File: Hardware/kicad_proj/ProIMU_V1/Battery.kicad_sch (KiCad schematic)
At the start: 19 parts, among them Q1 2SC4213

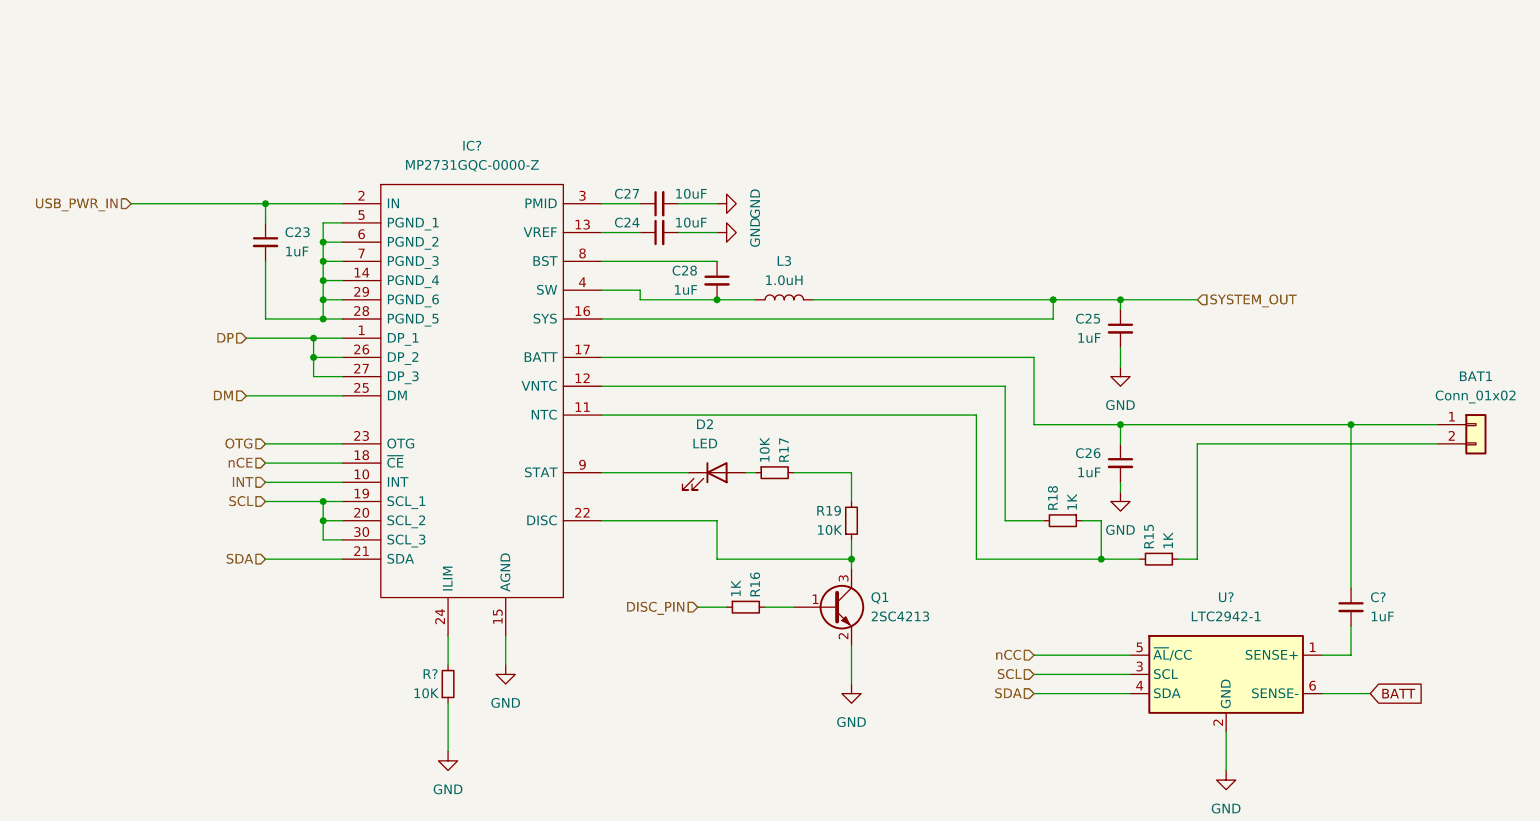
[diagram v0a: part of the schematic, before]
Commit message: Updated Schematic and Layout. RS232 and CAN connectors to be interchanged
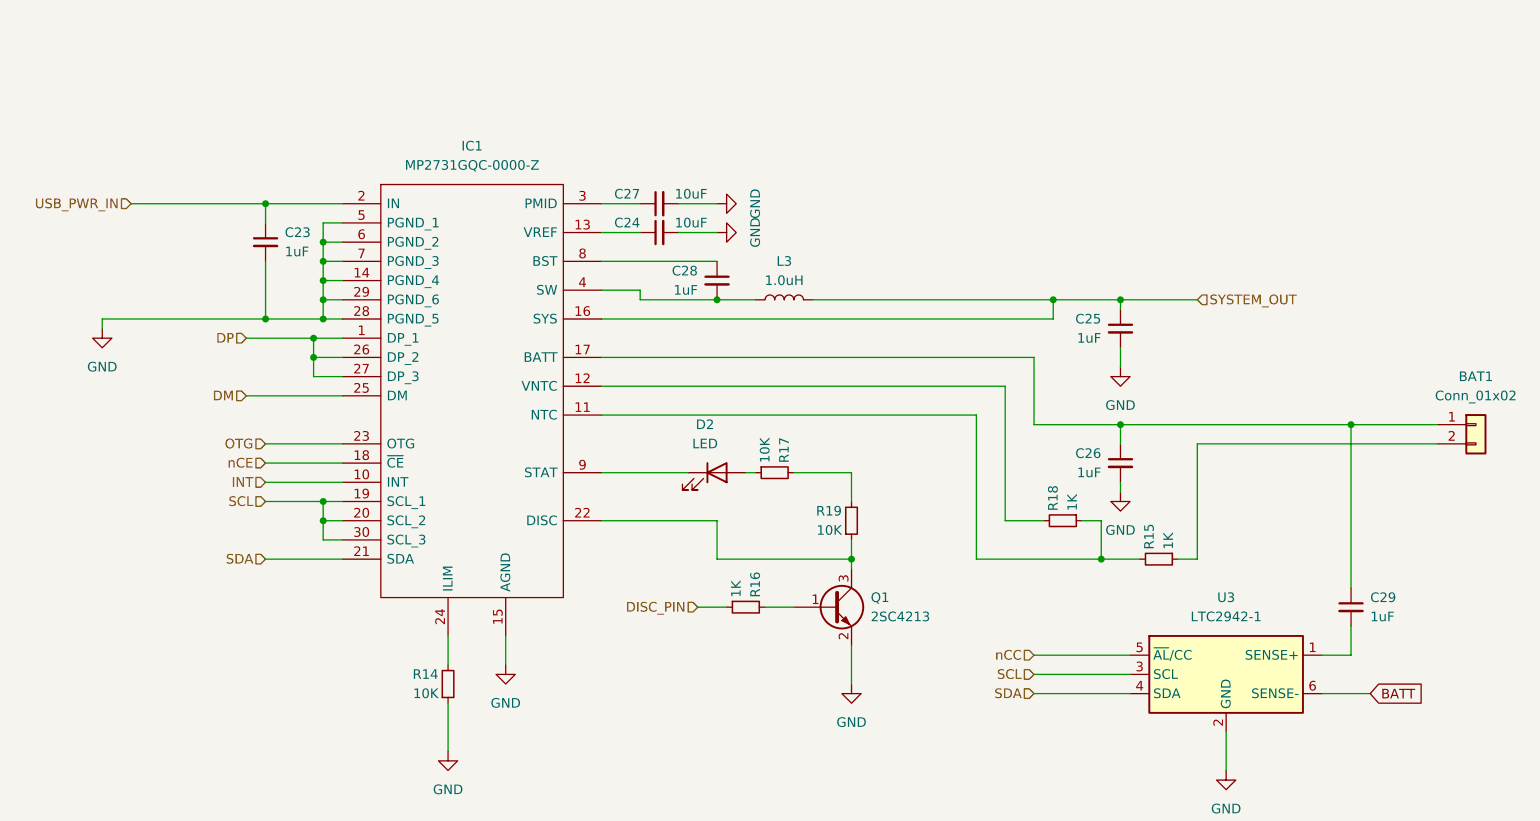
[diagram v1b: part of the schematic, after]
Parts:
- gave numbers to parts that had none: 4
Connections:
- net GND: now also C23.2, IC1.14 (PGND_4), IC1.28 (PGND_5), IC1.29 (PGND_6), IC1.5 (PGND_1), IC1.6 (PGND_2), IC1.7 (PGND_3)
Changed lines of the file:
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@@
   (junction (at 92.71 96.52) (diameter 0) (color 0 0 0 0)
   )
+  (junction (at 85.09 72.39) (diameter 0) (color 0 0 0 0)
+  )
   (junction (at 91.44 77.47) (diameter 0) (color 0 0 0 0)
   )
@@
     (stroke (width 0) (type default) (color 0 0 0 0))
   )
+  (wire (pts (xy 63.5 72.39) (xy 63.5 73.66))
+    (stroke (width 0) (type default) (color 0 0 0 0))
+  )
   (wire (pts (xy 142.24 110.49) (xy 146.05 110.49))
     (stroke (width 0) (type default) (color 0 0 0 0))
@@
   )
   (wire (pts (xy 92.71 64.77) (xy 92.71 67.31))
+    (stroke (width 0) (type default) (color 0 0 0 0))
+  )
+  (wire (pts (xy 85.09 72.39) (xy 63.5 72.39))
     (stroke (width 0) (type default) (color 0 0 0 0))
   )
@@
   (symbol (lib_id "power:GND") (at 212.09 132.08 0) (unit 1)
     (in_bom yes) (on_board yes) (fields_autoplaced)
-    (property "Reference" "#PWR?" (id 0) (at 212.09 138.43 0)
+    (property "Reference" "#PWR012" (id 0) (at 212.09 138.43 0)
       (effects (font (size 1.27 1.27)) hide)
     )
@@
     (pin "2")
   )
+  (symbol (lib_id "power:GND") (at 63.5 73.66 0) (unit 1)
+    (in_bom yes) (on_board yes) (fields_autoplaced)
+    (property "Reference" "#PWR08" (id 0) (at 63.5 80.01 0)
+      (effects (font (size 1.27 1.27)) hide)
+    )
+    (property "Value" "GND" (id 1) (at 63.5 78.74 0))
+    (property "Footprint" "" (id 2) (at 63.5 73.66 0)
+      (effects (font (size 1.27 1.27)) hide)
+    )
+    (property "Datasheet" "" (id 3) (at 63.5 73.66 0)
+      (effects (font (size 1.27 1.27)) hide)
+    )
+    (pin "1")
+  )
   (symbol (lib_id "Device:R_Small") (at 109.22 120.65 0) (mirror x) (unit 1)
     (in_bom yes) (on_board yes)
-    (property "Reference" "R?" (id 0) (at 107.95 119.38 0)
+    (property "Reference" "R14" (id 0) (at 107.95 119.38 0)
       (effects (font (size 1.27 1.27)) (justify right))
     )
@@
   (symbol (lib_id "power:GND") (at 116.84 118.11 0) (unit 1)
     (in_bom yes) (on_board yes) (fields_autoplaced)
-    (property "Reference" "#PWR?" (id 0) (at 116.84 124.46 0)
+    (property "Reference" "#PWR011" (id 0) (at 116.84 124.46 0)
       (effects (font (size 1.27 1.27)) hide)
     )
@@
   (symbol (lib_name "MP2731GQC-0000-Z_1") (lib_id "MP2731GQC-0000-Z:MP2731GQC-0000-Z") (at 96.52 57.15 0) (unit 1)
     (in_bom yes) (on_board yes) (fields_autoplaced)
-    (property "Reference" "IC?" (id 0) (at 112.395 49.53 0))
+    (property "Reference" "IC1" (id 0) (at 112.395 49.53 0))
     (property "Value" "MP2731GQC-0000-Z" (id 1) (at 112.395 52.07 0))
     (property "Footprint" "MP2731GQC0000Z" (id 2) (at 125.73 54.61 0)
@@
   (symbol (lib_id "Device:C_Small") (at 228.6 110.49 0) (unit 1)
     (in_bom yes) (on_board yes) (fields_autoplaced)
-    (property "Reference" "C?" (id 0) (at 231.14 109.2262 0)
+    (property "Reference" "C29" (id 0) (at 231.14 109.2262 0)
       (effects (font (size 1.27 1.27)) (justify left))
     )
@@
   (symbol (lib_id "Battery_Management:LTC2942-1") (at 212.09 119.38 0) (unit 1)
     (in_bom yes) (on_board yes) (fields_autoplaced)
-    (property "Reference" "U?" (id 0) (at 212.09 109.22 0))
+    (property "Reference" "U3" (id 0) (at 212.09 109.22 0))
     (property "Value" "LTC2942-1" (id 1) (at 212.09 111.76 0))
     (property "Footprint" "Package_DFN_QFN:DFN-6-1EP_3x2mm_P0.5mm_EP1.65x1.35mm" (id 2) (at 212.09 110.49 0)
@@
   (symbol (lib_id "power:GND") (at 109.22 129.54 0) (unit 1)
     (in_bom yes) (on_board yes) (fields_autoplaced)
-    (property "Reference" "#PWR?" (id 0) (at 109.22 135.89 0)
-      (effects (font (size 1.27 1.27)) hide)
-    )
+    (property "Reference" "#PWR010" (id 0) (at 109.22 135.89 0)
+      (effects (font (size 1.27 1.27)) hide)
+    )

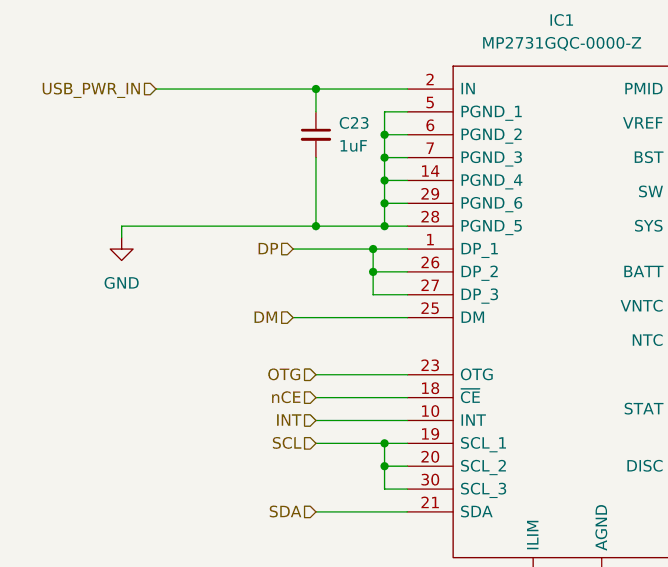
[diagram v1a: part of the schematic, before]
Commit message: Updated Schematic and Layout. Connectors and SD Card Port changed.
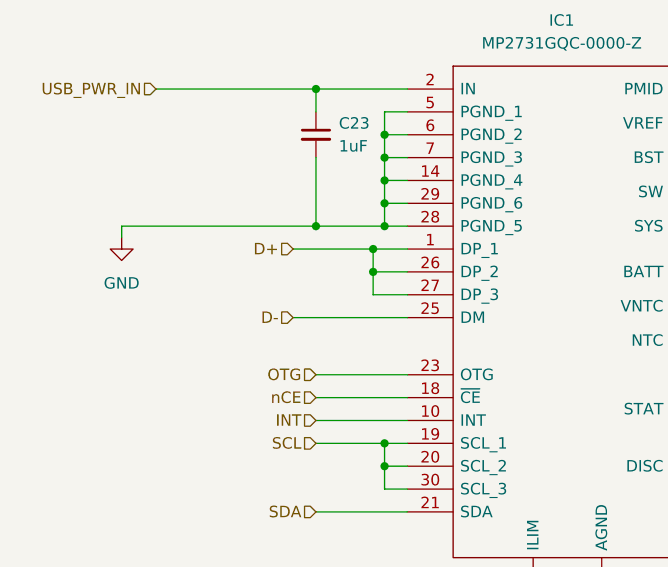
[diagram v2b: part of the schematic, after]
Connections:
- net DM renamed D-
- net DP renamed D+
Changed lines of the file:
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@@
     )
   )
-  (hierarchical_label "DP" (shape input) (at 82.55 74.93 180)
+  (hierarchical_label "D+" (shape input) (at 82.55 74.93 180)
     (effects (font (size 1.27 1.27)) (justify right))
   )
@@
     (effects (font (size 1.27 1.27)) (justify right))
   )
-  (hierarchical_label "DM" (shape input) (at 82.55 82.55 180)
+  (hierarchical_label "D-" (shape input) (at 82.55 82.55 180)
     (effects (font (size 1.27 1.27)) (justify right))
   )

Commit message: Updated Layout. Last commit for the day
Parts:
- IC1: footprint MP2731GQC0000Z -> footprints:MP2731GQC0000Z
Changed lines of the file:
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@@
     (property "Reference" "IC1" (id 0) (at 112.395 49.53 0))
     (property "Value" "MP2731GQC-0000-Z" (id 1) (at 112.395 52.07 0))
-    (property "Footprint" "MP2731GQC0000Z" (id 2) (at 125.73 54.61 0)
+    (property "Footprint" "footprints:MP2731GQC0000Z" (id 2) (at 125.73 54.61 0)
       (effects (font (size 1.27 1.27)) (justify left) hide)
     )

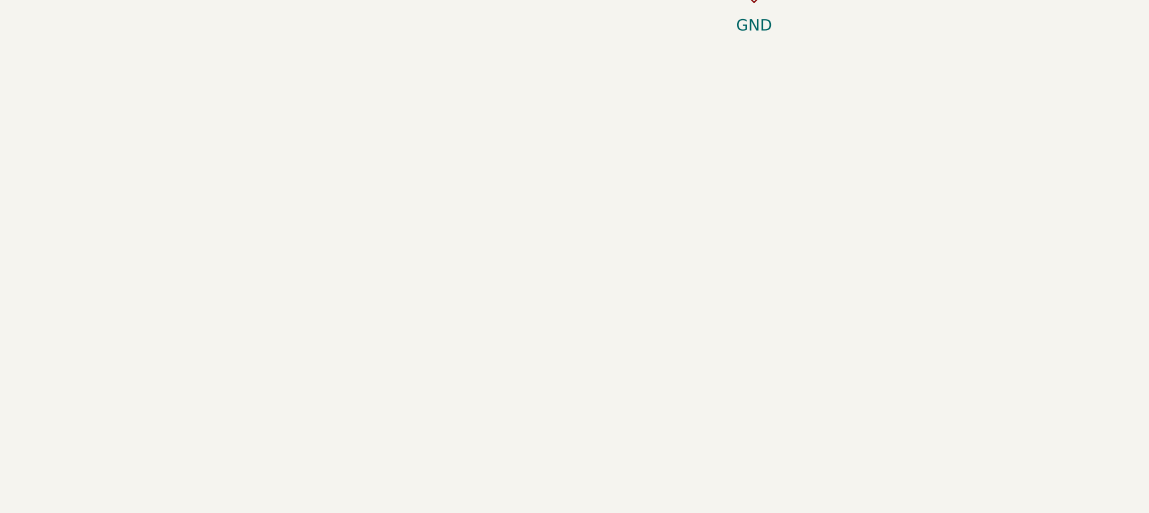
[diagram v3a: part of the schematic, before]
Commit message: Updated schematic. Added new isoalted dc/dc converter. Charger circuit needs to be updated
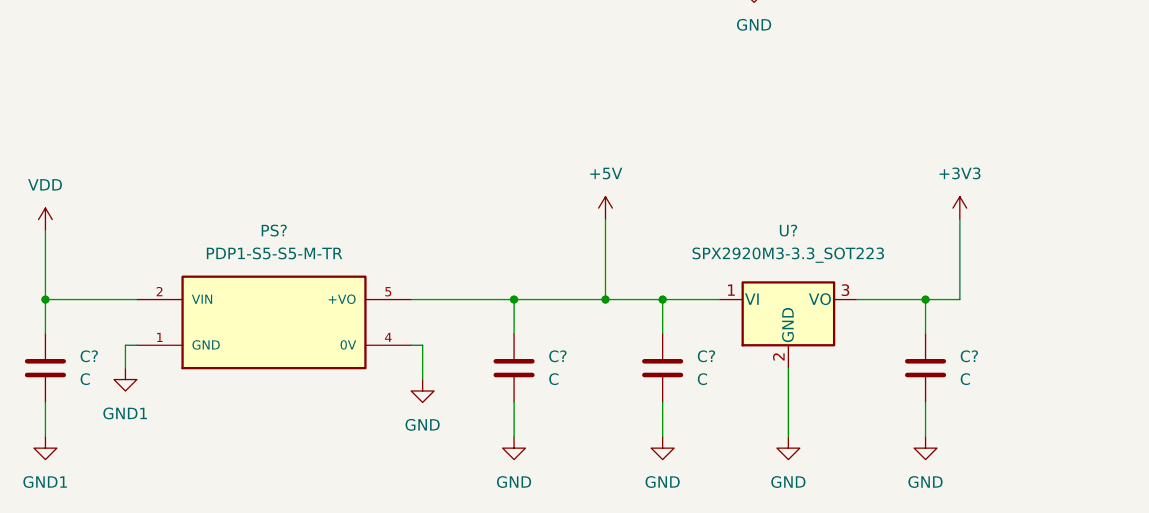
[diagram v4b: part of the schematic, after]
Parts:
- added C? (x4): C, symbol Device:C
- added PS?: PDP1-S5-S5-M-TR, footprints:CONV_PDP1-S5-S5-M-TR, symbol PDP1-S5-S5-M-TR:PDP1-S5-S5-M-TR
- added U?: SPX2920M3-3.3_SOT223, Package_TO_SOT_SMD:SOT-223-3_TabPin2, symbol Regulator_Linear:SPX2920M3-3.3_SOT223
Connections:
- net GND: now also C?.2, C?.2, C?.2, PS?.4 (0V), U?.2 (GND)
- new net +3V3: C?.1, U?.3 (VO)
- new net +5V: C?.1, C?.1, PS?.5 (+VO), U?.1 (VI)
- new net GND1: C?.2, PS?.1 (GND)
- new net VDD: C?.1, PS?.2 (VIN)

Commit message: Updated schematic and layout
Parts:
- BAT1: footprint Connector_PinSocket_2.54mm:PinSocket_1x02_P2.54mm_Vertical -> Connector_PinHeader_2.54mm:PinHeader_1x02_P2.54mm_Vertical
- C12, C13, C14, C15: renamed from C?; footprint (none) -> Capacitor_SMD:C_0805_2012Metric_Pad1.18x1.45mm_HandSolder
- gave numbers to parts that had none: 2
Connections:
- net at R15.1: no longer BAT1.2 (Pin_2)
- net at C26.1, C29.1, IC1.17 (BATT): no longer BAT1.1 (Pin_1)
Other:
- moved on the sheet: BAT1, C12, C13, C14, C15, C23, C24, C25, C26, C27, C28, C29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

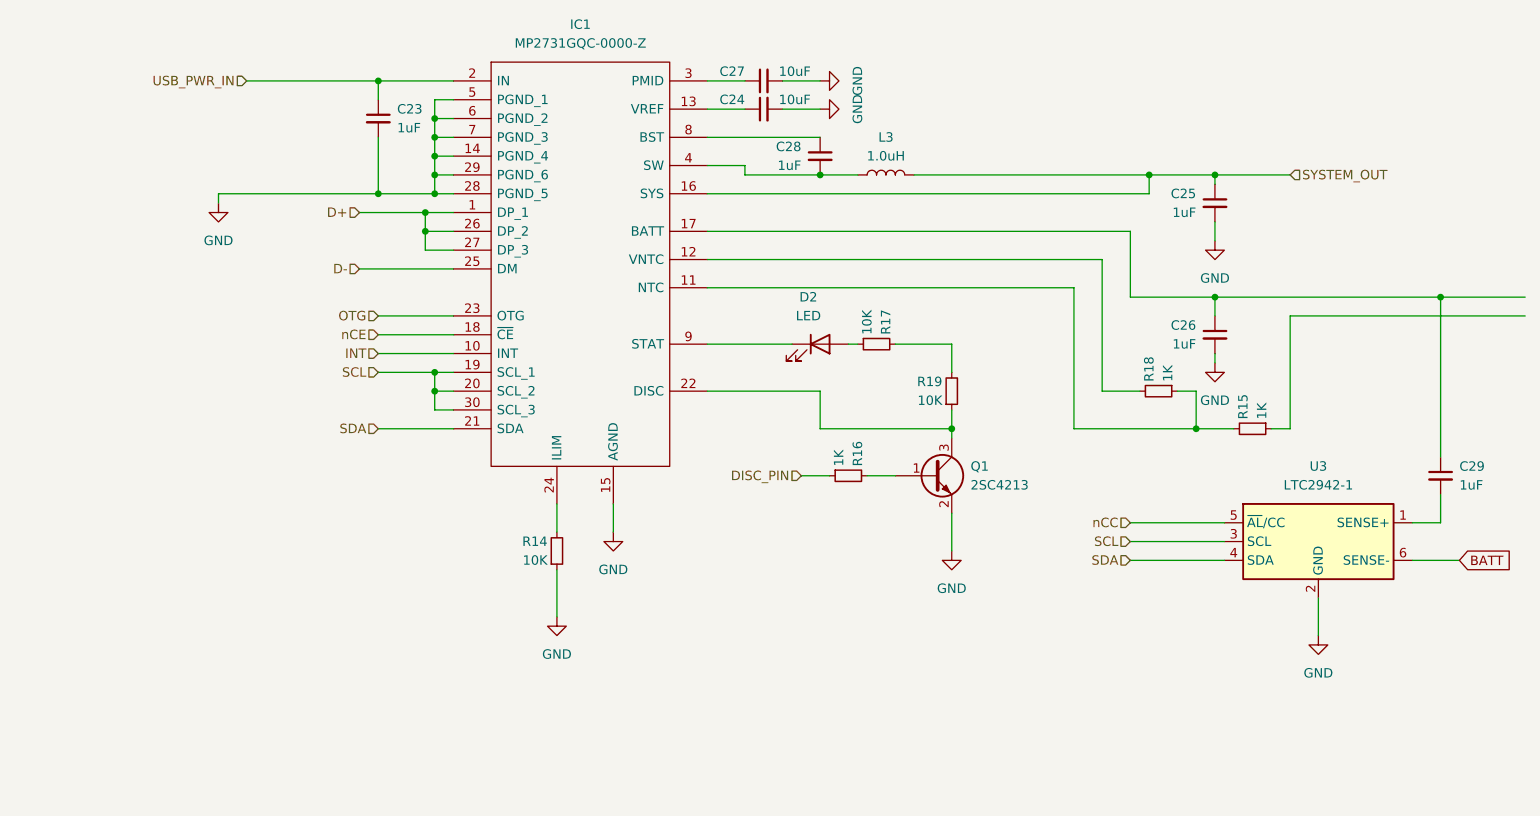
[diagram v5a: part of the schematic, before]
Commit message: Updated schematic and layout
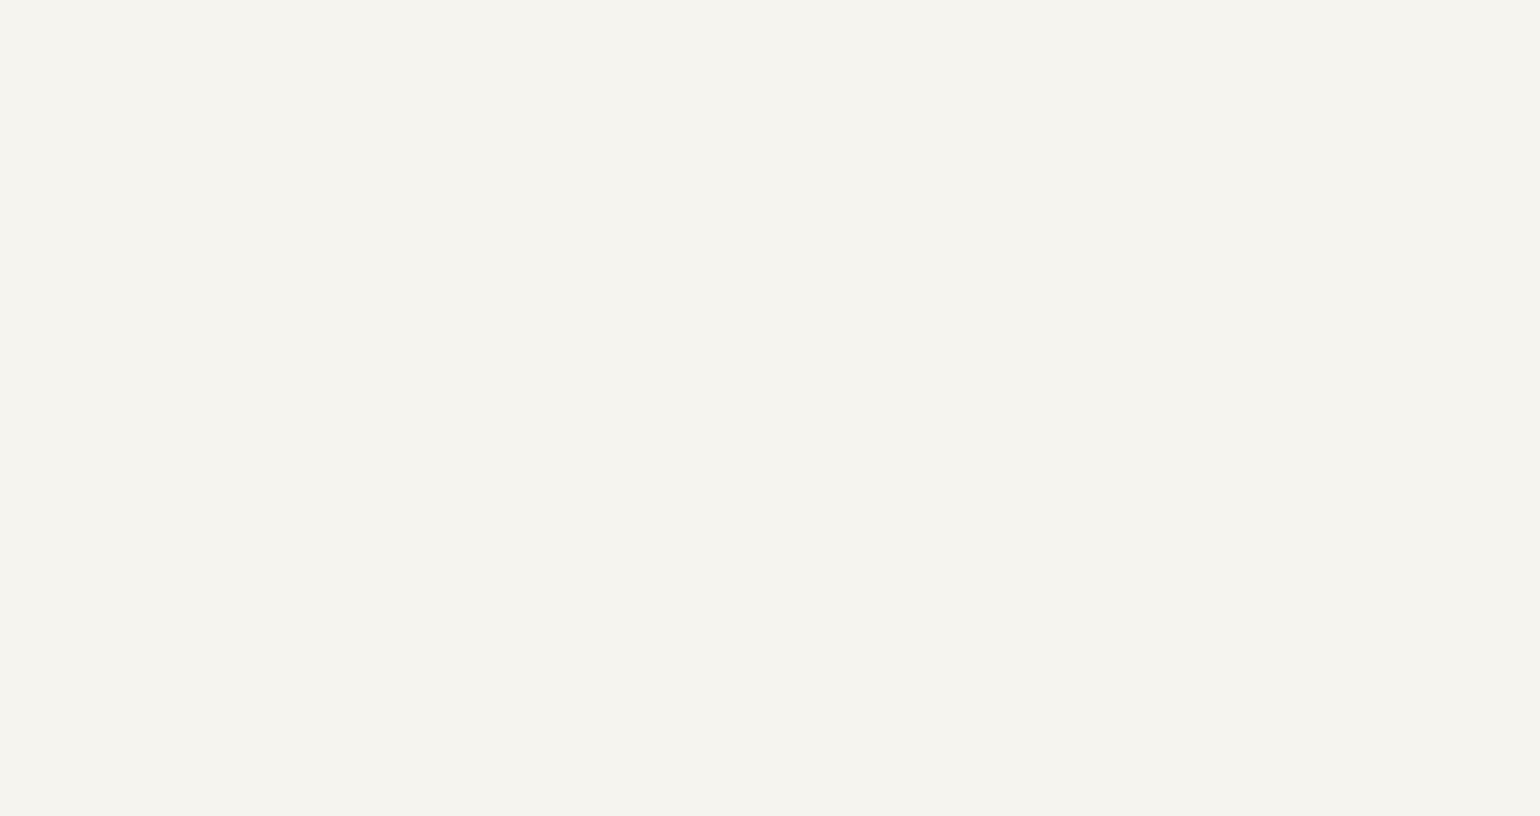
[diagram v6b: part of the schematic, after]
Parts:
- removed C23, C25, C26, C28, C29: 1uF, Capacitor_SMD:C_0402_1005Metric_Pad0.74x0.62mm_HandSolder, symbol Device:C_Small
- removed C24, C27: 10uF, Capacitor_SMD:C_0402_1005Metric_Pad0.74x0.62mm_HandSolder, symbol Device:C_Small
- removed D2: LED, LED_SMD:LED_0603_1608Metric, symbol Device:LED
- removed IC1: MP2731GQC-0000-Z, footprints:MP2731GQC0000Z, symbol MP2731GQC-0000-Z:MP2731GQC-0000-Z
- removed L3: 1.0uH, Inductor_SMD:L_0805_2012Metric_Pad1.05x1.20mm_HandSolder, symbol Device:L
- removed Q1: 2SC4213, Package_TO_SOT_SMD:SOT-323_SC-70, symbol Transistor_BJT:2SC4213
- removed R14, R17, R19: 10K, Resistor_SMD:R_0402_1005Metric_Pad0.72x0.64mm_HandSolder, symbol Device:R_Small
- removed R15, R16, R18: 1K, Resistor_SMD:R_0402_1005Metric_Pad0.72x0.64mm_HandSolder, symbol Device:R_Small
- removed U3: LTC2942-1, Package_DFN_QFN:DFN-6-1EP_3x2mm_P0.5mm_EP1.65x1.35mm, symbol Battery_Management:LTC2942-1
